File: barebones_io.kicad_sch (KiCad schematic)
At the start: 140 parts, among them IC1 W25Q80DVSSIG, IC2 W25Q80DVSSIG, J1 12401610E4_2A, J10 G45AA1912100B1EU, J13 SM02B-GHS-TB_LF__SN_, J14 SM02B-GHS-TB_LF__SN_, J2 12401610E4_2A, J3 1-2199119-5, J4 21992304, J5 G45AA1912100B1EU, J6 1040310811, J7 54-00007, J8 SJ2-35894B-SMT-TR, J9 54-00007, U16 TPS65987DDHRSHR, U17 TPS65987DDHRSHR, U19 TXS0104EYZTR, U21 TXS0104EYZTR, U25 TPD4E05U06DQAR, U26 TPD4E004DRYR, U42 TXS0104EYZTR, U43 TPS2553DBVR, U44 TPS2553DBVR, U45 PCA9306DCTR, U46 TPS2553DBVR, U47 TPS2553DBVR, U48 PCA9306DCTR

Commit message: Fixed version control merge issues
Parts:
- removed C219, C220: 100uF, Capacitor_SMD:C_0201_0603Metric, symbol Device:C
- removed C221: 0.1uF, Capacitor_SMD:C_0201_0603Metric, symbol Device:C
- removed D12, D13, D14: TPD4E02B04DQAR, barebones:DIO_TPD4E02B04DQAR, symbol TPD4E02B04DQAR:TPD4E02B04DQAR
- removed J10: G45AA1912100B1EU, barebones:AMPHENOL_G45AA1912100B1EU, symbol G45AA1912100B1EU:G45AA1912100B1EU
- removed R130: 27k, Resistor_SMD:R_0402_1005Metric, symbol Device:R
- removed R131, R132, R135, R136, R137, R138, R139: 2.2k, Resistor_SMD:R_0402_1005Metric, symbol Device:R
- removed R133: 18k, Resistor_SMD:R_0402_1005Metric, symbol Device:R
- removed R134, R140: 10k, Resistor_SMD:R_0402_1005Metric, symbol Device:R
- removed R141: 330k, Resistor_SMD:R_0402_1005Metric, symbol Device:R
- removed U47: TPS2553DBVR, barebones:SOT95P280X145-6N, symbol TPS2553DBVR:TPS2553DBVR
- removed U48: PCA9306DCTR, barebones:SOP65P400X130-8N, symbol PCA9306DCTR:PCA9306DCTR
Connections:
- net TMDS_CLOCK_1_DM: no longer D11.2 (IO2)
- net TMDS_CLOCK_1_DP: no longer D11.1 (IO1)
- net TMDS_DATA0_1_DM: no longer D11.5 (IO4)
- net TMDS_DATA0_1_DP: no longer D11.4 (IO3)
- no-connect marks 103 -> 102
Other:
- moved on the sheet: C112, C216, C217, C218, D11, J5, J6, R118, R119, R120, R121, R122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

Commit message: Day 8 updated files
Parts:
- removed C112: 10uF, Capacitor_SMD:C_0201_0603Metric, symbol Device:C
- added C219: 10uF, Capacitor_SMD:C_0201_0603Metric, symbol Device:C
- added C220, C221: 100uF, Capacitor_SMD:C_0201_0603Metric, symbol Device:C
- added C222: 0.1uF, Capacitor_SMD:C_0201_0603Metric, symbol Device:C
- added D12, D13, D14: TPD4E02B04DQAR, barebones:DIO_TPD4E02B04DQAR, symbol TPD4E02B04DQAR:TPD4E02B04DQAR
- added J10: 10067847-001RLF, 10067847-001RLF:AMPHENOL_10067847-001RLF, symbol 10067847-001RLF:10067847-001RLF
- added J11: G45AA1912100B1EU, barebones:AMPHENOL_G45AA1912100B1EU, symbol G45AA1912100B1EU:G45AA1912100B1EU
- added R130: 27k, Resistor_SMD:R_0402_1005Metric, symbol Device:R
- added R131, R132, R135, R136, R137, R138, R139: 2.2k, Resistor_SMD:R_0402_1005Metric, symbol Device:R
- added R133: 18k, Resistor_SMD:R_0402_1005Metric, symbol Device:R
- added R134, R140: 10k, Resistor_SMD:R_0402_1005Metric, symbol Device:R
- added R141: 330k, Resistor_SMD:R_0402_1005Metric, symbol Device:R
- added U47: PCA9306DCTR, barebones:SOP65P400X130-8N, symbol PCA9306DCTR:PCA9306DCTR
- added U48: TPS2553DBVR, barebones:SOT95P280X145-6N, symbol TPS2553DBVR:TPS2553DBVR
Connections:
- net GND: now also C220.1, C221.1, C222.1, D12.3 (GND), D12.8 (GND), D13.3 (GND), D13.8 (GND), D14.3 (GND), D14.8 (GND), J10.3 (VSS), J10.6 (VSS), J10.G1 (GND), J10.G2 (GND), J11.11 (TMDS_CLOCK_SHIELD), J11.17 (DDC/CEC_GROUND), J11.2 (TMDS_DATA2_SHIELD), J11.5 (TMDS_DATA1_SHIELD), J11.8 (TMDS_DATA0_SHIELD), J11.SH1 (SHIELD), J11.SH2 (SHIELD), J11.SH3 (SHIELD), J11.SH4 (SHIELD), R134.2, R141.2, U47.1 (GND), U48.2 (GND); no longer J6.10 (SW_DETECT), J6.6 (VSS)
- net HDMI2_1_5V0: now also C221.2, C222.2, J11.18 (+5V_POWER), U48.6 (OUT); no longer C216.2, C217.2, J5.18 (+5V_POWER), U46.6 (OUT)
- net HDMI2_1_FAULT: now also R140.1, U48.4 (~{FAULT}); no longer R118.1, U46.4 (~{FAULT})
- net HDMI_1_CEC: now also C220.2, J11.13 (CEC), R130.2; no longer C218.2, J5.13 (CEC), R127.2
- net HDMI_1_SCL: now also R132.2, U47.3 (SCL1); no longer R120.2, U45.3 (SCL1)
- net HDMI_1_SCL_1: now also J11.15 (SCL), R131.2, R137.2, U47.6 (SCL2); no longer J5.15 (SCL), R122.2, R128.2
- net HDMI_1_SDA: now also R135.2, U47.4 (SDA1); no longer R121.2, U45.4 (SDA1)
- net HDMI_1_SDA_1: now also J11.16 (SDA), R136.2, R138.2, U47.5 (SDA2); no longer J5.16 (SDA), R123.2, R129.2, U45.5 (SDA2)
- net HDMI_HPD_1V8_1: now also R133.2, R134.1; no longer R125.2, R126.1
- net HOT_PLUG_DETECT_1: now also J11.19 (HOT_PLUG_DETECT), R133.1; no longer J5.19 (HOT_PLUG_DETECT), R125.1
- net SD_CLK: now also J10.5 (CLK); no longer J6.5 (CLK)
- net SD_CMD: now also J10.2 (CMD); no longer J6.3 (CMD)
- net SD_DAT0: now also J10.7 (DAT0); no longer J6.7 (DAT0)
- net SD_DAT1: now also J10.8 (DAT1); no longer J6.8 (DAT1)
- net SD_DAT2: now also J10.9 (DAT2); no longer J6.1 (DAT2)
- net SD_DAT3: now also J10.1 (DAT3/CD); no longer J6.2 (CD/DAT3)
- net SD_DETECT: now also J10.CD; no longer J6.9 (SW_DETECT_2)
- net TMDS_CLOCK_1_DM: now also D14.2 (IO2), J11.12 (TMDS_CLOCK-); no longer J5.12 (TMDS_CLOCK-)
- net TMDS_CLOCK_1_DP: now also D14.1 (IO1), J11.10 (TMDS_CLOCK+); no longer J5.10 (TMDS_CLOCK+)
- net TMDS_DATA0_1_DM: now also D14.5 (IO4), J11.9 (TMDS_DATA0-); no longer J5.9 (TMDS_DATA0-)
- net TMDS_DATA0_1_DP: now also D14.4 (IO3), J11.7 (TMDS_DATA0+); no longer J5.7 (TMDS_DATA0+)
- net TMDS_DATA1_1_DM: now also D13.5 (IO4), J11.6 (TMDS_DATA1-); no longer J5.6 (TMDS_DATA1-)
- net TMDS_DATA1_1_DP: now also D13.4 (IO3), J11.4 (TMDS_DATA1+); no longer J5.4 (TMDS_DATA1+)
- net TMDS_DATA2_1_DM: now also D13.2 (IO2), J11.3 (TMDS_DATA2-); no longer J5.3 (TMDS_DATA2-)
- net TMDS_DATA2_1_DP: now also D13.1 (IO1), J11.1 (TMDS_DATA2+); no longer J5.1 (TMDS_DATA2+)
- net USB3_ENABLE: no longer U46.3 (EN)
- net VCC_1V8_SYS: now also R132.1, R135.1, U47.2 (VREF1)
- net VCC_3V3_SYS: now also C219.2, R130.1, R140.2
- net VCC_5V0_PERIPH: now also R131.1, R136.1, R137.1, R138.1, R139.1, R139.2, U47.7 (VREF2), U47.8 (EN), U48.1 (IN)
- net TMDS_DATA2_0_DP: now reaches D11.1 (IO1)
- net TMDS_DATA2_0_DP: now also J5.1 (TMDS_DATA2+)
- net TMDS_DATA2_0_DM: now reaches D11.2 (IO2)
- net TMDS_DATA2_0_DM: now also J5.3 (TMDS_DATA2-)
- net TMDS_DATA1_0_DP: now reaches D11.4 (IO3)
- net TMDS_DATA1_0_DP: now also J5.4 (TMDS_DATA1+)
- net TMDS_DATA1_0_DM: now reaches D11.5 (IO4)
- net TMDS_DATA1_0_DM: now also J5.6 (TMDS_DATA1-)
- new net: C219.1, J10.4 (VDD)
- new net: R141.1, U48.5 (ILIM)
- new net: D14.10 (NC), D14.6 (NC), D14.7 (NC), D14.9 (NC)
- new net: D13.10 (NC), D13.6 (NC), D13.7 (NC), D13.9 (NC)
- new net: D12.10 (NC), D12.6 (NC), D12.7 (NC), D12.9 (NC)
- new net HDMI2_0_5V0: C216.2, C217.2, J5.18 (+5V_POWER), U46.6 (OUT)
- new net HDMI2_0_FAULT: R118.1, U46.4 (~{FAULT})
- new net HDMI_0_CEC: C218.2, J5.13 (CEC), R127.2
- new net HDMI_0_SCL: R120.2, U45.3 (SCL1)
- new net HDMI_0_SCL_1: J5.15 (SCL), R122.2, R128.2
- new net HDMI_0_SDA: R121.2, U45.4 (SDA1)
- new net HDMI_0_SDA_1: J5.16 (SDA), R123.2, R129.2, U45.5 (SDA2)
- new net HDMI_ENABLE: U46.3 (EN), U48.3 (EN)
- new net HDMI_HPD_1V8_0: R125.2, R126.1
- new net HOT_PLUG_DETECT_0: J5.19 (HOT_PLUG_DETECT), R125.1
- new net SD_WRITE_PROT: J10.WP
- new net TMDS_CLOCK_0_DM: D12.2 (IO2), J5.12 (TMDS_CLOCK-)
- new net TMDS_CLOCK_0_DP: D12.1 (IO1), J5.10 (TMDS_CLOCK+)
- new net TMDS_DATA0_0_DM: D12.5 (IO4), J5.9 (TMDS_DATA0-)
- new net TMDS_DATA0_0_DP: D12.4 (IO3), J5.7 (TMDS_DATA0+)
- no-connect marks 102 -> 107
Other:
- note added: "SD CARD SLOT"
- note removed: "MICRO SD CARD SLOT"
- moved on the sheet: C216, C217, C218, D11, J5, R118, R119, R120, R121, R122, R123, R124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

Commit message: fixed the power distribution by adding RK806 chips
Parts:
- removed R55, R56: 10k, Resistor_SMD:R_0402_1005Metric, symbol Device:R
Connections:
- net USB_CTRL_RESET_1: now reaches U16.44 (HRESET)
- net USB_CTRL_RESET_2: now reaches U17.44 (HRESET)
- removed net TYPEC0_SBU1: D10.4 (IO3), D10.5 (IO4), D9.4 (IO3), J1.A8 (SBU1), J2.A8 (SBU1), J2.B8 (SBU2)
- net TYPEC0_SBU2 renamed USB_1_SBU2
- net TYPEC0_SSRX1N/DP0_RX0N renamed USB_1_RX1N
- net TYPEC0_SSRX1N/DP0_TX0N renamed USB_2_RX1N
- net TYPEC0_SSRX1P/DP0_RX0P renamed USB_1_RX1P
- net TYPEC0_SSRX1P/DP0_TX0P renamed USB_2_RX1P
- net TYPEC0_SSRX2N/DP0_RX2N renamed USB_1_RX2N
- net USB_1_RX2N: no longer D6.1 (IO1), J2.A10 (RX2-)
- net TYPEC0_SSRX2P/DP0_RX2P renamed USB_1_RX2P
- net USB_1_RX2P: no longer D6.2 (IO2), J2.A11 (RX2+)
- net TYPEC0_SSTX1N/DP0_TX1N renamed USB_1_TX1N
- net USB_1_TX1N: no longer C94.1
- net TYPEC0_SSTX1P/DP0_TX1P renamed USB_1_TX1P
- net USB_1_TX1P: no longer C93.1
- net TYPEC0_SSTX2N/DP0_TX3N renamed USB_1_TX2N
- net USB_1_TX2N: no longer C97.2
- net TYPEC0_SSTX2P/DP0_TX3P renamed USB_1_TX2P
- net USB_1_TX2P: no longer C98.2
- net TYPEC0_USB20_OTG_DM renamed USB_1_OTG_DM
- net USB_1_OTG_DM: no longer D10.2 (IO2), J2.A7 (D1-), J2.B7 (D2-)
- net TYPEC0_USB20_OTG_DP renamed USB_1_OTG_DP
- net USB_1_OTG_DP: no longer D10.1 (IO1), J2.A6 (D1+), J2.B6 (D2+)
- new net USB_1_SBU1: D9.4 (IO3), J1.A8 (SBU1)
- new net USB_2_OTG_DM: D10.2 (IO2), J2.A7 (D1-), J2.B7 (D2-)
- new net USB_2_OTG_DP: D10.1 (IO1), J2.A6 (D1+), J2.B6 (D2+)
- new net USB_2_RX2N: D6.1 (IO1), J2.A10 (RX2-)
- new net USB_2_RX2P: D6.2 (IO2), J2.A11 (RX2+)
- new net USB_2_SBU1: D10.4 (IO3), J2.A8 (SBU1)
- new net USB_2_SBU2: D10.5 (IO4), J2.B8 (SBU2)
- new net USB_2_TX1N: C94.1
- new net USB_2_TX1P: C93.1
- new net USB_2_TX2N: C97.2
- new net USB_2_TX2P: C98.2
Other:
- note added: "USE A CHEAPER ESD FOR THE 2.0 LINES"
- note removed: "TYPEC0_SSRX1P/DP0_TX0P"

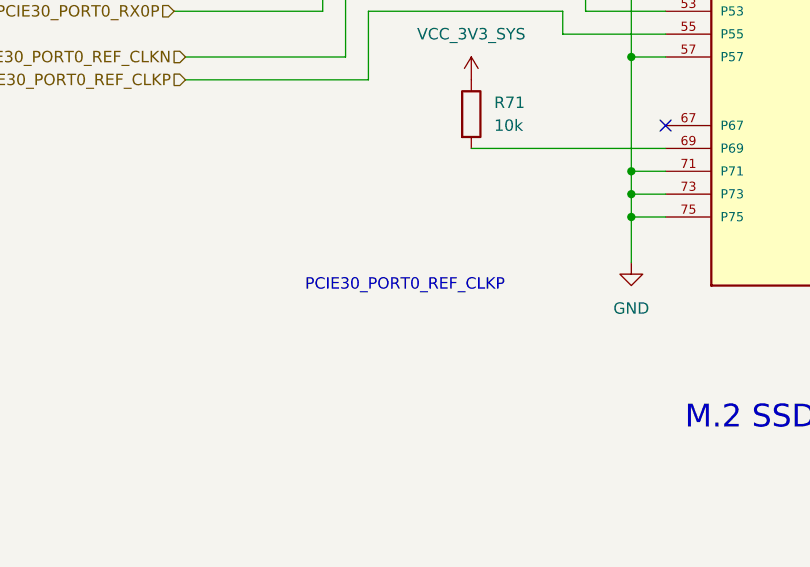
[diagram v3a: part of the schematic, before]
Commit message: routed the two 64Gb LPDDR4x RAM chips
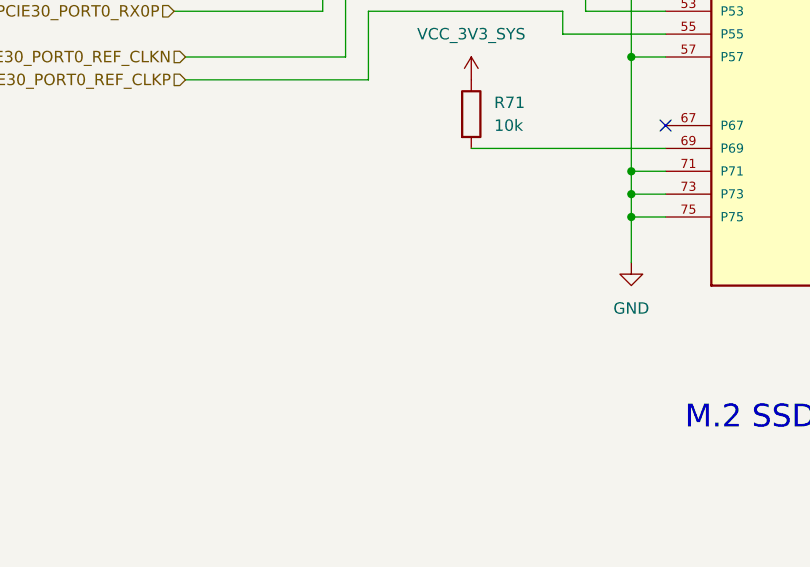
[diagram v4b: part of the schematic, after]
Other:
- note removed: "PCIE30_PORT0_REF_CLKP"
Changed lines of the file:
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@@
-		)
-	)
-	(text "PCIE30_PORT0_REF_CLKP"
-		(exclude_from_sim no)
-		(at 701.294 152.4 0)
-		(effects
-			(font
-				(size 1.27 1.27)
-			)
 		)
 	)

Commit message: added a USB 3.1 hub for the Type-A ports and a CLK generator for the PCIE 3.0/2.0
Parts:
- removed C100, C101, C102, C107, C108, C99: 100nF, Capacitor_SMD:C_0201_0603Metric, symbol Device:C
- removed C212, C213, C214, C215: 0.1uF, Capacitor_SMD:C_0201_0603Metric, symbol Device:C
- removed D10, D9: TPD4E02B04DQAR, barebones:DIO_TPD4E02B04DQAR, symbol TPD4E02B04DQAR:TPD4E02B04DQAR
- removed R71, R75, R76: 10k, Resistor_SMD:R_0402_1005Metric, symbol Device:R
- added C391, C392, C393, C394: 220nF, Capacitor_SMD:C_0201_0603Metric, symbol Device:C
- added C399, C400, C401, C402, C403, C404, C415, C430, C439, C440: 100nF, Capacitor_SMD:C_0201_0603Metric, symbol Device:C
- added C416, C417, C418, C451, C456, C457, C458, C459, C460, C461, C462, C463, C464, C468, C469, C470, C471, C472, C473, C474, C475, C476, C477, C478, C479, C480, C481, C482, C483, C484, C485, C486: 0.1uF, Capacitor_SMD:C_0201_0603Metric, symbol Device:C
- added C428, C429, C447, C448, C452, C453: 12pF, Capacitor_SMD:C_0201_0603Metric, symbol Device:C
- added C441, C449: 1uF, Capacitor_SMD:C_0201_0603Metric, symbol Device:C
- added C450: 4.7uF, Capacitor_SMD:C_0201_0603Metric, symbol Device:C
- added J12: 1-2199119-5, barebones:TE_1-2199119-5, symbol 1-2199119-5:1-2199119-5
- added L17: XAL7030-472MEB, XAL7030-472MEB:IND_XAL7030-472MEB, symbol XAL7030-472MEB:XAL7030-472MEB
- added R170: 475R, Resistor_SMD:R_0402_1005Metric, symbol Device:R
- added R171, R172, R184, R193, R195, R196, R197, R198, R199, R201, R202, R203, R204: 10k, Resistor_SMD:R_0402_1005Metric, symbol Device:R
- added R175, R200: 2.2R, Resistor_SMD:R_0402_1005Metric, symbol Device:R
- added R176, R177, R178, R179, R180, R181, R182, R183: 50R, Resistor_SMD:R_0402_1005Metric, symbol Device:R
- added R185, R186, R187, R188, R189, R190, R191, R192: 33R, Resistor_SMD:R_0402_1005Metric, symbol Device:R
- added R194: 6.81k, Resistor_SMD:R_0402_1005Metric, symbol Device:R
- added TP10: MISO, TestPoint:TestPoint_Pad_D1.5mm, symbol Connector:TestPoint
- added TP7: CHIP SELECT, TestPoint:TestPoint_Pad_D1.5mm, symbol Connector:TestPoint
- added TP8: CLOCK, TestPoint:TestPoint_Pad_D1.5mm, symbol Connector:TestPoint
- added TP9: MOSI, TestPoint:TestPoint_Pad_D1.5mm, symbol Connector:TestPoint
- added U52: PI6C557-05LEX, easyeda2kicad:TSSOP-20_L6.5-W4.4-P0.65-LS6.4-BL, symbol PI6C557-05LEX:PI6C557-05LEX
- added U53: PI6C557-05BLEX, barebones:TSSOP-20_L6.5-W4.4-P0.65-LS6.4-BL, symbol PI6C557-05BLEX:PI6C557-05BLEX
- added U54, U56, U57: TPD4E004DRYR, barebones:PSON50P145X100X60-6N, symbol TPD4E004DRYR:TPD4E004DRYR
- added U55: PI6C557-03ALEX, easyeda2kicad:TSSOP-16_L5.0-W4.4-P0.65-LS6.4-BL, symbol PI6C557-03ALEX:PI6C557-03ALEX
- added U58: GL3523-ONY30, barebones:QFN-48_L6.0-W6.0-P0.40-BL-EP3.8, symbol GL3523-ONY30:GL3523-ONY30
- added U59: 9FGV0641AKILFT, barebones:WQFN-40_L5.0-W5.0-P0.40-TL-EP3.5, symbol 9FGV0641AKILFT:9FGV0641AKILFT
- added Y2, Y3, Y4: C2E-25.000-10-1530-X-R, barebones:XTAL_C2E-25.000-10-1530-X-R, symbol C2E-25.000-10-1530-X-R:C2E-25.000-10-1530-X-R
- C103, C104, C105, C106: value 100nF -> 220nF
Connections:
- net GND: now also U26.3 (GND), C399.1, C400.1, C401.1, C402.1, C403.1, C404.1, C416.1, C417.1, C428.1, C429.1, C430.1, C439.1, C440.1, C441.1, C447.1, C448.1, C449.1, C450.1, C451.1, C452.1, C453.1, C468.2, C469.2, C470.2, C471.2, C472.2, C473.2, C474.2, C475.2, C476.2, C477.2, C478.2, C479.2, C480.2, C481.2, C482.2, C483.2, C484.2, C485.2, C486.2, J12.1 (P1), J12.15 (P15), J12.21 (P21), J12.27 (P27), J12.3 (P3), J12.33 (P33), J12.39 (P39), J12.45 (P45), J12.51 (P51), J12.57 (P57), J12.71 (P71), J12.73 (P73), J12.75 (P75), J12.9 (P9), J12.SH1 (SHIELD), J12.SH2 (SHIELD), R170.2, R176.2, R177.2, R178.2, R179.2, R180.2, R181.2, R182.2, R183.2, R194.1, R195.2, R201.2, U53.16 (GNDODA), U53.2 (S0), U53.3 (S1), U53.4 (S2), U53.9 (GNDXD), U54.3 (GND), U56.3 (GND), U57.3 (GND), U58.23 (VSSP), U58.35 (PGANG), U58.49 (EP), U59.1 (SS_EN_tri), U59.13 (~{OE0}), U59.21 (~{OE1}), U59.24 (~{OE2}), U59.30 (~{OE3}), U59.35 (~{OE4}), U59.38 (~{VOE5}), U59.41 (GND), U59.8 (GNDDIG), Y2.2 (GND), Y2.4 (GND), Y3.2 (GND), Y3.4 (GND), Y4.2 (GND), Y4.4 (GND)
- net PCIE20_0_REFCLKN: now also U59.36 (DIF5); no longer J4.49
- net PCIE20_0_REFCLKP: now also U59.37 (~{DIF5}); no longer J4.47
- net PCIE20_0_TXN: now also J4.43
- net PCIE20_0_TXP: now also J4.41
- net PCIE30_PORT0_REF_CLKN: now also R182.1, R188.2, U59.15 (~{DIF0}); no longer J3.53 (P53)
- net PCIE30_PORT0_REF_CLKP: now also R183.1, R187.2, U59.14 (DIF0); no longer J3.55 (P55)
- net PCIE30_PORT0_RX0N: now also J3.41 (P41); no longer J3.47 (P47)
- net PCIE30_PORT0_RX0P: now also J3.43 (P43); no longer J3.49 (P49)
- net PCIE30_PORT0_RX1P: no longer J3.29 (P29)
- net PCIE30_PORT1_RX0N: now also J12.41 (P41); no longer J3.17 (P17)
- net PCIE30_PORT1_RX0P: now also J12.43 (P43); no longer J3.19 (P19)
- net PCIE30_PORT1_RX1N: now also J12.29 (P29); no longer J3.5 (P5)
- net PCIE30_PORT1_RX1P: now also J12.31 (P31); no longer J3.7 (P7)
- net PCIE30_PORT1_TX0N: now also C393.1
- net PCIE30_PORT1_TX0P: now also C394.1
- net PCIE30_PORT1_TX1N: now also C391.1
- net PCIE30_PORT1_TX1P: now also C392.1
- net USB3_0_DN: now also D3.14 (D1P), U58.16 (DM_P2); no longer D3.13 (D1N)
- net USB3_0_DP: now also D3.13 (D1N), U58.15 (DP_P2); no longer D3.14 (D1P)
- net USB3_0_RX_N: now also C462.2
- net USB3_0_RX_P: now also C461.2
- net USB3_0_TX_N: now also C458.2, U58.13 (RXN1_P2); no longer J7.8 (SSTX-)
- net USB3_0_TX_P: now also C457.1, U58.14 (RXP1_P2); no longer J7.9 (SSTX+)
- net USB3_1_DN: now also U58.4 (DM_P3)
- net USB3_1_DP: now also U58.3 (DP_P3)
- net USB3_1_RX_N: now also C460.2
- net USB3_1_RX_P: now also C459.2
- net USB3_1_TX_N: now also C418.2, U58.8 (RXN1_P3); no longer J9.8 (SSTX-)
- net USB3_1_TX_P: now also C456.1, U58.9 (RXP1_P3); no longer J9.9 (SSTX+)
- net USB_1_OTG_DM: now also U26.2
- net USB_1_OTG_DP: now also U26.1
- net USB_1_SBU1: now also U26.4
- net USB_1_SBU2: now also U26.5
- net USB_2_OTG_DM: now also U54.2
- net USB_2_OTG_DP: now also U54.1
- net USB_2_SBU1: now also U54.4
- net USB_2_SBU2: now also U54.5
- net VCC_1V8_SYS: now also C478.1, C479.1, C480.1, C481.1, C482.1, C483.1, C484.1, C485.1, C486.1, R200.1, R202.1, R203.1, R204.1, U59.11 (VDDDIG1.8), U59.16 (VDD1.8), U59.17 (VDDIO), U59.27 (VDDIO), U59.31 (VDD1.8), U59.32 (VDDIO), U59.39 (VDDIO), U59.4 (VDDXTAL1.8), U59.5 (VDDREF1.8)
- net VCC_3V3_SYS: now also U26.6 (VCC), C416.2, C417.2, R184.1, R195.1, U54.6 (VCC); no longer C219.2, J3.12 (P12), J3.14 (P14), J3.16 (P16), J3.18 (P18), J3.2 (P2), J3.4 (P4), J3.70 (P70), J3.72 (P72), J3.74 (P74)
- net VCC_5V0_PERIPH: now also U58.25 (VDDP)
- net at C105.2: now also J3.47 (P47); no longer J3.41 (P41)
- net at C106.2: now also J3.49 (P49); no longer J3.43 (P43)
- net PCIE30X4_WAKEn_M1_L: now reaches J3.54 (P54)
- net at C219.1, J10.4 (VDD): now also C415.1
- net at J4.8: now also R184.2
- net PCIE30X4_CLKREQN_M0 renamed PCIE30X4_CLKREQn_M1_L
- net PCIE30X4_PERSTN_M0 renamed PCIE30X4_PERSTn_M1_L
- net SD_CLK renamed SDMMC_CLK
- net SDMMC_CLK: now also U57.1
- net SD_CMD renamed SDMMC_CMD
- net SDMMC_CMD: now also U57.2
- net SD_DAT0 renamed SDMMC_DAT0
- net SDMMC_DAT0: now also U57.4
- net SD_DAT1 renamed SDMMC_DAT1
- net SDMMC_DAT1: now also U57.5
- net SD_DAT2 renamed SDMMC_DAT2
- net SDMMC_DAT2: now also U56.1
- net SD_DAT3 renamed SDMMC_DAT3
- net SDMMC_DAT3: now also U56.2
- net SD_DETECT renamed SDMMC_DET
- net SD_WRITE_PROT: no longer names the net of J10.WP
- net USB20_HOST0_DN renamed USB20_HOST0_DM
- net USB3_0_FAULT renamed GL_USB30_FAULT_0
- net GL_USB30_FAULT_0: now also R196.2, U58.20 (OVCUR2J)
- net USB3_1_FAULT renamed GL_USB30_FAULT_1
- net GL_USB30_FAULT_1: now also R198.2, U58.19 (OVCUR3J)
- net USB3_ENABLE renamed GL_USB30_EN_0
- net GL_USB30_EN_0: now also R197.2, U58.21 (PWREN2J); no longer U44.3 (EN)
- new net: R192.1, U53.13 (~{CLK2})
- new net: R185.1, U53.11 (~{CLK3})
- new net: C463.2, U58.44 (TXP1_P0)
- new net: R171.2, U53.7 (~{PD})
- new net: R186.1, U53.12 (CLK3)
- new net: C428.2, U53.5 (X1), Y2.3
- new net: R202.2, U59.40 (~{CKPWRGD_PD})
- new net: R170.1, U53.10 (IREF)
- new net: R191.1, U53.14 (CLK2)
- new net: C440.2, C441.2, R175.1, U53.15 (VDDODA)
- new net: R190.1, U53.17 (~{CLK1})
- new net: R189.1, U53.18 (CLK1)
- new net: R188.1, U53.19 (~{CLK0})
- new net: R187.1, U53.20 (CLK0)
- new net: C429.2, U53.6 (X2), Y2.1
- new net: R172.2, U53.8 (OE)
- new net: C393.2, J12.47 (P47)
- new net: C418.1, J9.8 (SSTX-)
- new net: C461.1, U58.10 (TXN1_P2)
- new net: C456.2, J9.9 (SSTX+)
- new net: C462.1, U58.11 (TXP1_P2)
- new net: C464.2, U58.43 (TXN1_P0)
- new net: C460.1, U58.5 (TXN1_P3)
- new net: C459.1, U58.6 (TXP1_P3)
- new net: R201.1, U59.6 (SADR/REF1.8)
- new net: C458.1, J7.8 (SSTX-)
- new net: C457.2, J7.9 (SSTX+)
- new net: C391.2, J12.35 (P35)
- new net: C392.2, J12.37 (P37)
- new net: C394.2, J12.49 (P49)
- new net GL_RESETJ: C449.2, R193.2, U58.30 (RESETJ)
- new net GL_RTERM: R194.2, U58.28 (RTERM)
- new net GL_SPI_CK: TP9.1, U58.32 (P_SPI_CK)
- new net GL_SPI_CZ: TP7.1, U58.34 (P_SPI_CZ)
- new net GL_SPI_D0: TP10.1, U58.31 (P_SPI_DO)
- new net GL_SPI_DI: TP8.1, U58.33 (P_SPI_DI)
- new net GL_SW: L17.1, U58.24 (SW)
- new net GL_USB30_EN_1: R199.2, U44.3 (EN), U58.18 (PWREN3J)
- new net GL_X1: C447.2, U58.39 (X1), Y3.3
- new net GL_X2: C448.2, U58.38 (X2), Y3.1
- new net PCIE20_0_REFCLKN_SLOT: J4.49, U59.33 (DIF4)
- new net PCIE20_0_REFCLKP_SLOT: J4.47, U59.34 (~{DIF4})
- new net PCIE30X2_CLKREQn_M1_L: J12.52 (P52)
- new net PCIE30X2_PERSTn_M1_L: J12.50 (P50)
- new net PCIE30X2_WAKEn_M1_L: J12.54 (P54)
- new net PCIE30_PORT0_RX1N: J3.29 (P29)
- new net PCIE30_PORT1_REF_CLKN: R180.1, R190.2, U59.19 (~{DIF1})
- new net PCIE30_PORT1_REF_CLKP: R181.1, R189.2, U59.18 (DIF1)
- new net PCIE30_REFCLKN_SLOT_0: J3.53 (P53), R178.1, R192.2, U59.23 (~{DIF2})
- new net PCIE30_REFCLKN_SLOT_1: J12.53 (P53), R176.1, R185.2, U59.29 (~{DIF3})
- new net PCIE30_REFCLKP_SLOT_0: J3.55 (P55), R179.1, R191.2, U59.22 (DIF2)
- new net PCIE30_REFCLKP_SLOT_1: J12.55 (P55), R177.1, R186.2, U59.28 (DIF3)
- new net SCLK_3.3_C: R203.2, U59.9 (SCLK_3.3)
- new net SDATA_3.3_C: R204.2, U59.10 (SDATA_3.3)
- new net USB20_HOST1_DM: U58.42 (DM_P0)
- new net USB20_HOST1_DP: U58.41 (DP_P0)
- new net USB30_2_SSRXN: C464.1
- new net USB30_2_SSRXP: C463.1
- new net USB30_2_SSTXN: U58.46 (RXN1_P0)
- new net USB30_2_SSTXP: U58.47 (RXP1_P0)
- new net VCC3V3_PCIE30: C399.2, C400.2, C401.2, J3.12 (P12), J3.14 (P14), J3.16 (P16), J3.18 (P18), J3.2 (P2), J3.4 (P4), J3.70 (P70), J3.72 (P72), J3.74 (P74)
- new net VCC3V3_PCIE30_1: C402.2, C403.2, C404.2, J12.12 (P12), J12.14 (P14), J12.16 (P16), J12.18 (P18), J12.2 (P2), J12.4 (P4), J12.70 (P70), J12.72 (P72), J12.74 (P74)
- new net VCC3V3_PI6C_05: C430.2, C439.2, R171.1, R172.1, R175.2, U53.1 (VDDXD)
- new net VCC_1V2_HUB: C473.1, C474.1, C475.1, C476.1, C477.1, L17.2, U58.1 (AVDD12), U58.12 (VP12_P2), U58.22 (FB), U58.29 (DVDD12), U58.45 (VP12_P0), U58.7 (VP12_P3)
- new net VCC_3V3_S3: C219.2, C415.2, C468.1, C469.1, C470.1, C471.1, C472.1, R193.1, R196.1, R197.1, R198.1, R199.1, U58.17 (AVDD33_3), U58.2 (AVDD33_2), U58.26 (V5), U58.27 (V33), U58.36 (VBUS), U58.37 (DVDD33), U58.40 (AVDD33_1), U58.48 (AVDD33)
- new net VDDA1.8_C: C450.2, C451.2, R200.2, U59.26 (VDDA1.8)
- new net VDDIO_C1: U59.12 (VDDIO)
- new net X1_C: C452.2, U59.2 (X1_25), Y4.3
- new net X2_C: C453.2, U59.3 (X2), Y4.1
- no-connect marks 107 -> 150
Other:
- note added: "1%"
- note added: "PRIMARY M.2 SSD SLOT"
- note added: "SECONDARY M.2 SSD SLOT"
- note added: "USE 1% TOLERANCE"
- note removed: "M.2 SSD SLOT"
- note removed: "USE A CHEAPER ESD FOR THE 2.0 LINES"
- moved on the sheet: C103, C216, C217, C218, C219, C220, C221, C222, C91, C92, C93, C94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
